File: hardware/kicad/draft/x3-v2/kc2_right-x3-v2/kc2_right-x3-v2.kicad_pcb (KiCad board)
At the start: 2 copper layers, 163.7 x 122.5 mm, 92 parts, among them SW1 KEY_01, SW10 KEY_10, SW11 KEY_11, SW12 KEY_12, SW13 KEY_13, SW14 KEY_14, SW15 KEY_15, SW16 KEY_16, SW17 KEY_17, SW18 KEY_18, SW19 KEY_19, SW2 KEY_02, SW20 KEY_20, SW21 KEY_21, SW22 KEY_22, SW23 KEY_23, SW24 KEY_24, SW25 KEY_25, SW26 KEY_26, SW27 KEY_27, SW28 KEY_28, SW29 KEY_29, SW3 KEY_03, SW30 KEY_30, SW31 KEY_31, SW32 KEY_32, SW33 KEY_33, SW34 KEY_34, SW35 KEY_35, SW36 KEY_36, SW37 KEY_37, SW38 KEY_38, SW39 KEY_39, SW4 KEY_04, SW5 KEY_05, SW6 KEY_06, SW7 KEY_07, SW8 KEY_08, SW9 KEY_09, U1 nice!nano_v2_socket_24pin

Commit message: feat(x3-v2): reinforce mounting holes
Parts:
- added MH9: M1.4_NPTH_1.60, MH_M1.4_NPTH_1.60, F.Cu at (177.5, 118.0)
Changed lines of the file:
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@@
+	(footprint "MH_M1.4_NPTH_1.60"
+		(layer "F.Cu")
+		(at 177.5 118)
+		(descr "KC2 X3 V2 M1.4 service mounting hole, 1.60 mm copper-free NPTH")
+		(tags "KC2 X3 V2 M1.4 mounting NPTH copper-free")
+		(property "Reference" "MH9"
+			(at 0 -1.5 0)
+			(layer "F.SilkS")
+			(effects
+				(font
+					(size 0.8 0.8)
+					(thickness 0.15)
+				)
+			)
+		)
+		(property "Value" "M1.4_NPTH_1.60"
+			(at 0 0 0)
+			(layer "F.Fab")
+			(hide yes)
+			(effects
+				(font
+					(size 0.8 0.8)
+					(thickness 0.1)
+				)
+			)
+		)
+		(property "Datasheet" ""
+			(at 0 0 0)
+			(layer "F.Fab")
+			(hide yes)
+			(effects
+				(font
+					(size 1.27 1.27)
+				)
+			)
+		)
+		(property "Description" ""
+			(at 0 0 0)
+			(layer "F.Fab")
+			(hide yes)
+			(effects
+				(font
+					(size 1.27 1.27)
+				)
+			)
+		)
+		(attr exclude_from_pos_files exclude_from_bom)
+		(duplicate_pad_numbers_are_jumpers no)
+		(pad "" np_thru_hole circle
+			(at 0 0)
+			(size 1.6 1.6)
+			(drill 1.6)
+			(layers "*.Mask")
+		)
+		(embedded_fonts no)
+	)
 	(footprint "MH_M1.4_NPTH_1.60"
 		(layer "F.Cu")

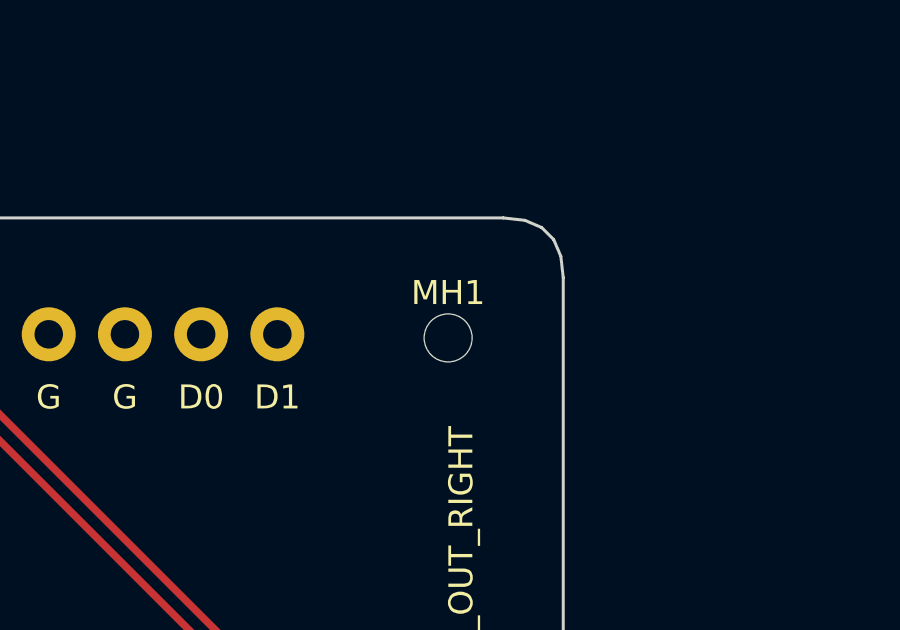
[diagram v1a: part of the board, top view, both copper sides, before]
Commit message: feat(x3-v2): prepare JLCPCB quote and diode evidence
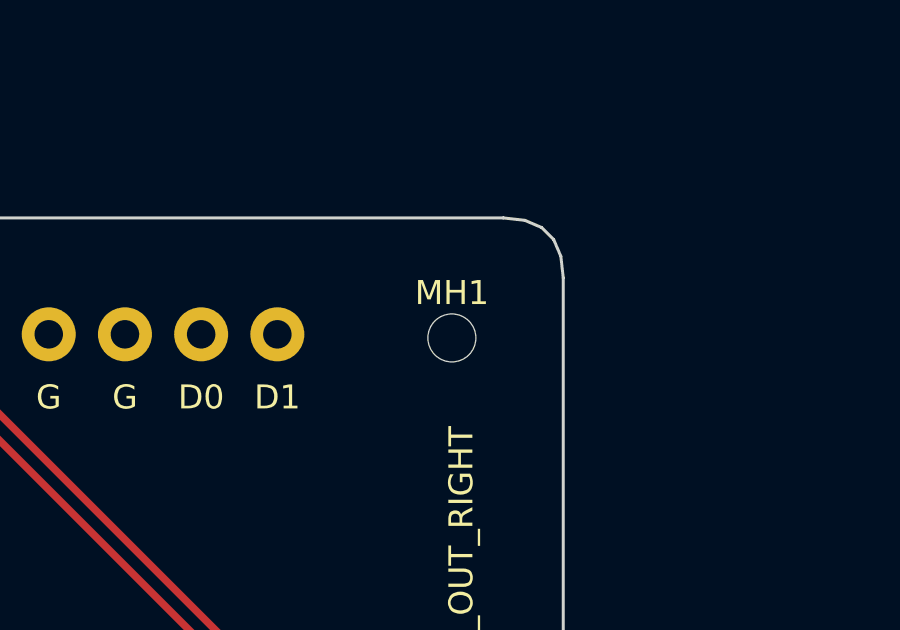
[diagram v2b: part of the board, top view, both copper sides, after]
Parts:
- moved MH1 0.12 mm to (97.2, 43.2)
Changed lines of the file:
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@@
 	(footprint "MH_M1.4_NPTH_1.60"
 		(layer "F.Cu")
-		(at 97.0625 43.25)
+		(at 97.1875 43.25)
 		(descr "KC2 X3 V2 M1.4 service mounting hole, 1.60 mm copper-free NPTH")
 		(tags "KC2 X3 V2 M1.4 mounting NPTH copper-free")

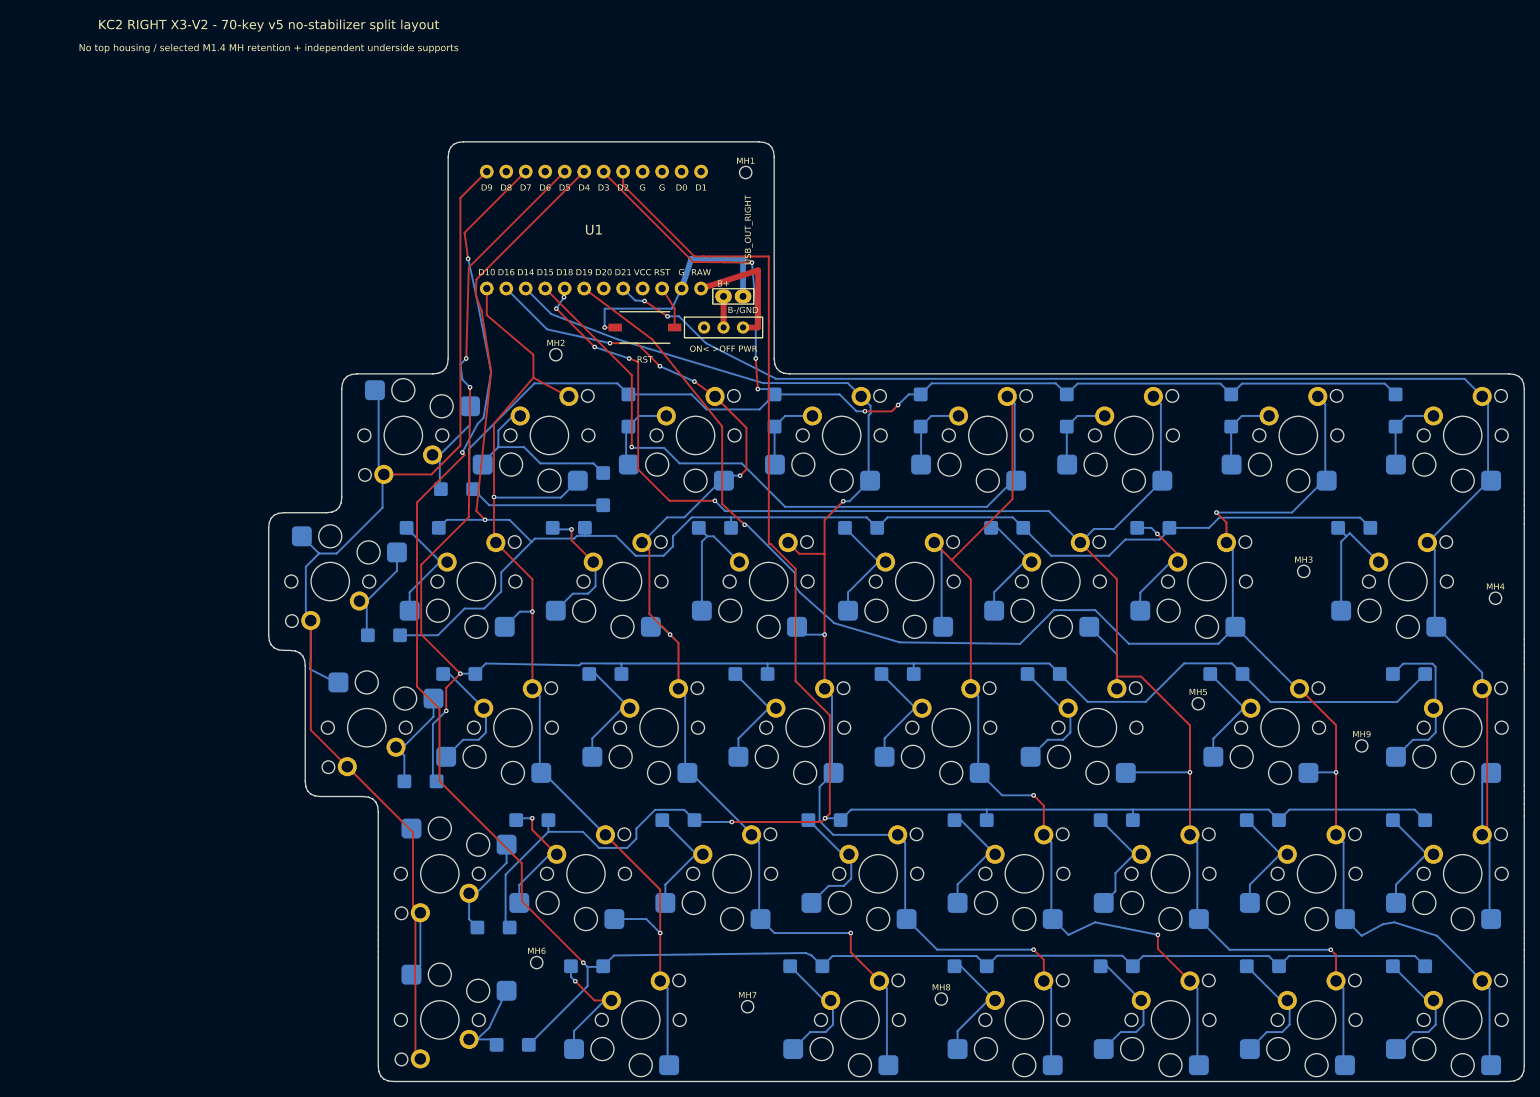
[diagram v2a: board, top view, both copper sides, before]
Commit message: feat(x3-v2): adopt 1N4148W and dense housing supports
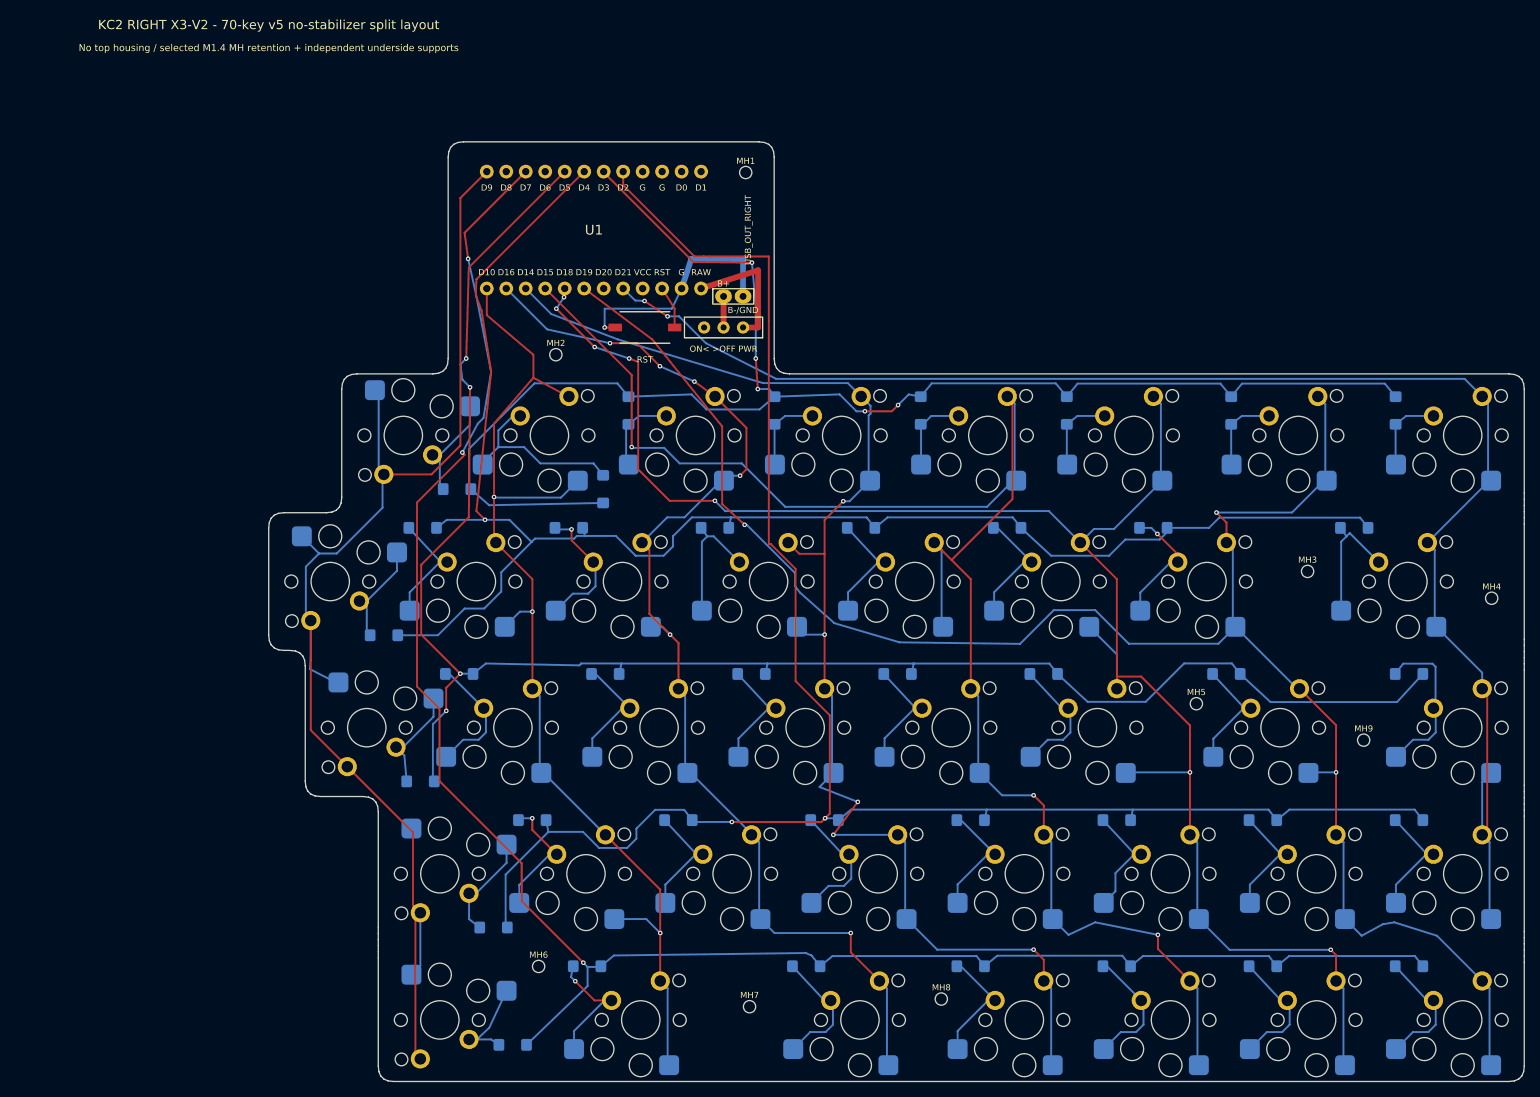
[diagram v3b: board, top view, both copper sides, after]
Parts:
- BAT1: value BAT_301230_30x12mm -> 301230_3.7V_100mAh; footprint KC2:BAT_301230_30x12mm -> BAT_301230_30x12mm
- D1, D10, D11, D12, D13, D14, D15, D16, D17, D18, D19, D2, D20, D21, D22, D23, D24, D25, D26, D27, D28, D29, D3, D30, D31, D32, D33, D34, D35, D36, D37, D38, D39, D4, D5, D6, D7, D8, D9: value ES1B_Jingdao_C437840_Eleparts9475342 -> 1N4148W-13-F_DiodesInc_SOD123; footprint D_ES1B_SMA_HandSolder_C437840 -> D_1N4148W_SOD123_HandSolder_DiodesInc
- J_BAT1: value BAT_2Pin_PTH_DirectSolder -> 301230_DIRECT_SOLDER; footprint KC2:BAT_2Pin_PTH_DirectSolder -> BAT_2Pin_PTH_DirectSolder
- SW_PWR1: value SW_IMMS_12V_BSI10_THT -> IMMS-12V_BSI-10; footprint KC2:SW_IMMS_12V_BSI10_THT -> SW_IMMS_12V_BSI10_THT
- moved MH9 0.79 mm to (177.8, 117.2)
- moved MH6 0.56 mm to (70.2, 146.8)
- moved MH3 0.50 mm to (170.4, 95.2)
- moved MH4 0.50 mm to (194.4, 98.8)
- moved MH5 0.25 mm to (155.9, 112.5)
- moved MH7 0.25 mm to (97.7, 152.0)
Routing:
- net R_COL3: track 173.6 -> 177.3 mm, vias 3 -> 5
- net R_ROW0: track 198.4 -> 200.1 mm
- net R_ROW1: track 211.4 -> 212.2 mm
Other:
- board text added: "Diode: Diodes Inc 1N4148W-13-F SOD-123; pad 1 = row cathode"
- board text removed: "Diode: Jingdao ES1B / C437840 / Eleparts 9475342; pad 1 = row cathode"
